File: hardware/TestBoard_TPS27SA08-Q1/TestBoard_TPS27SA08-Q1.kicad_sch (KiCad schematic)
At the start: 78 parts, among them J1 575-4, J10 Conn_01x04, J11 Conn_01x02, J12 Conn_01x02, J14 Conn_01x02, J15 Conn_01x06, J2 575-4, J3 575-4, J4 575-4, J7 Conn_01x02, J8 Conn_01x02, J9 Conn_01x02, Q1 SQJ141ELP, U1 TPS27SA08-Q1, U2 Logic Analyzer, U3 MCP23S17-E/SO, U4 NUCLEO_L432KC

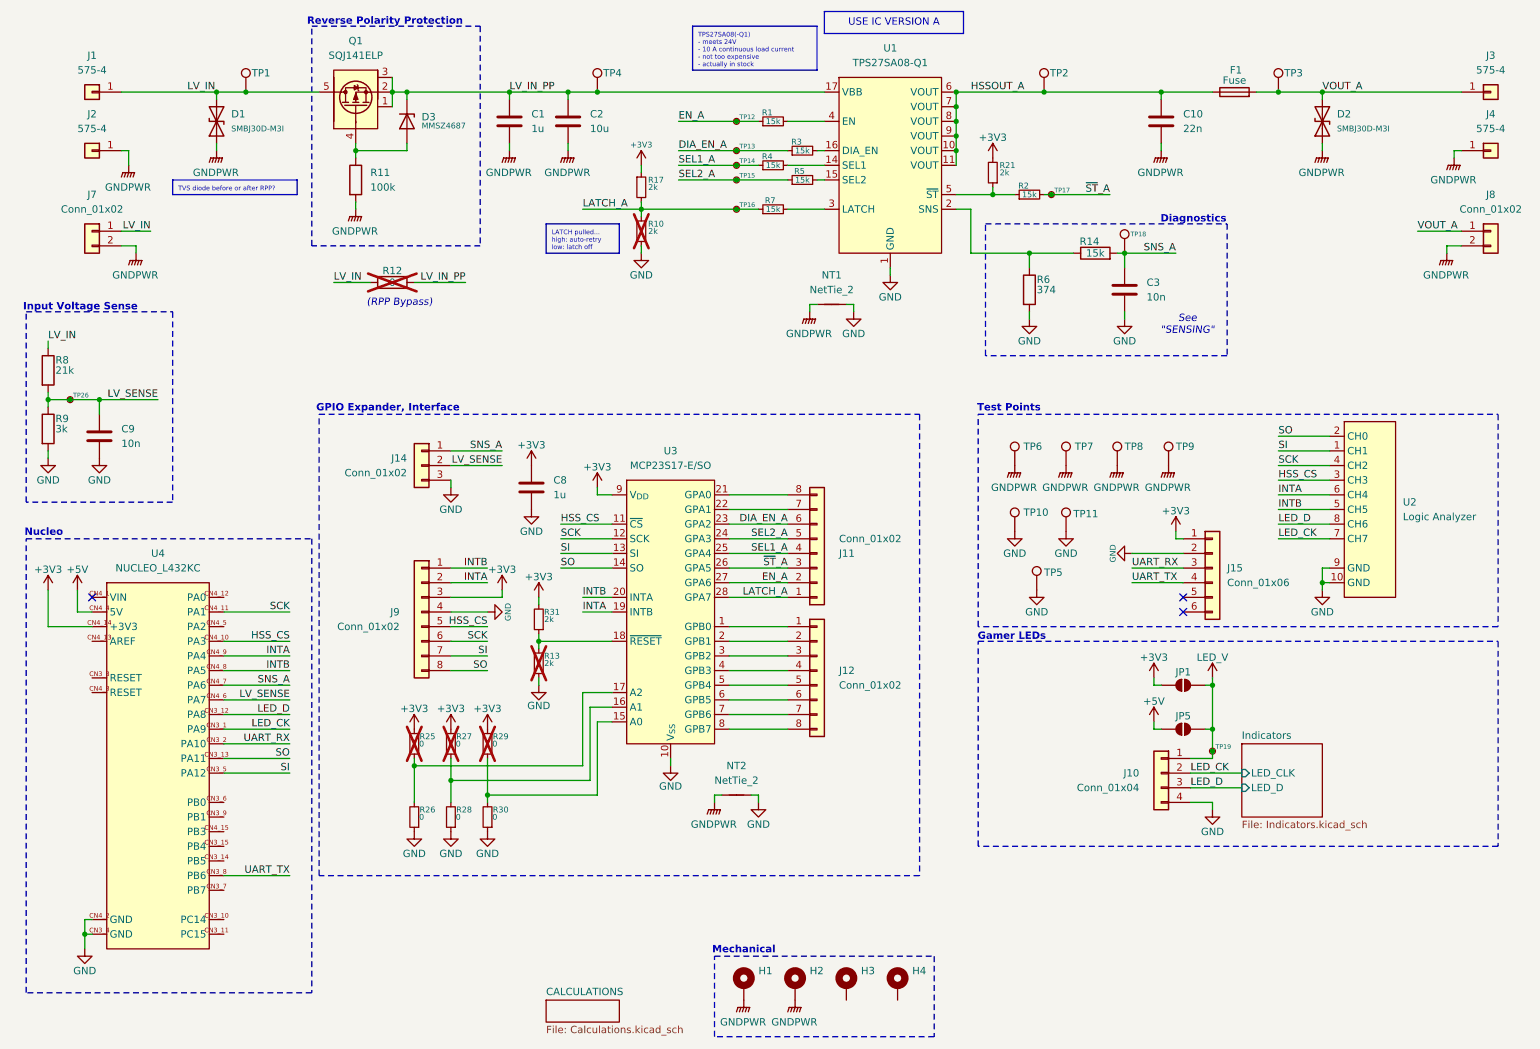
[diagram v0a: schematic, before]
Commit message: revisions (dip switch for address, leds on gpio outputs, logic analyzer pinout?, ...)
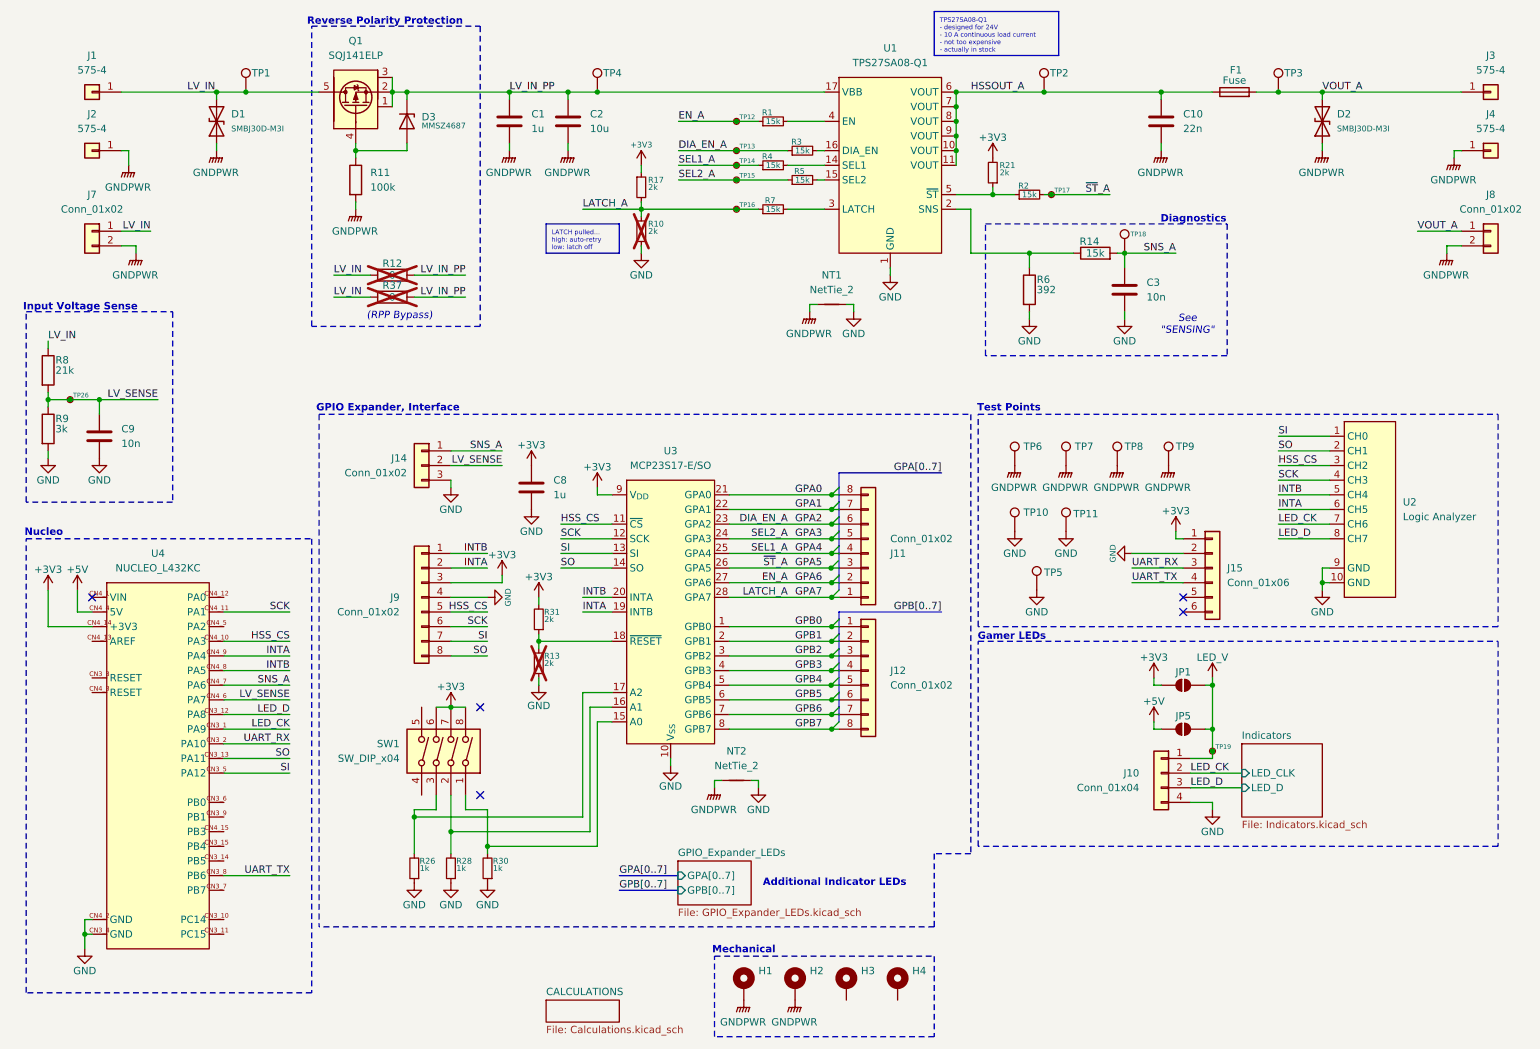
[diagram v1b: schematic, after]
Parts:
- removed R25, R27, R29: 0, Resistor_SMD:R_0805_2012Metric, symbol Device:R_Small
- added R37: 0, Resistor_SMD:R_0805_2012Metric, symbol Device:R
- added SW1: SW_DIP_x04, PowerDistributionUnitLib:ADE04S04, symbol Switch:SW_DIP_x04
- R26, R28, R30: value 0 -> 1k
- R6: value 374 -> 392
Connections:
- net +3V3: now also SW1.6, SW1.7, SW1.8
- net LV_IN: now also R37.1
- net LV_IN_PP: now also R37.2
- net at R30.2, U3.15 (A0): now also SW1.1
- net GPA1: now reaches J11.7 (Pin_7), U3.22 (GPA1)
- net GPA0: now reaches J11.8 (Pin_8), U3.21 (GPA0)
- net at R28.2, U3.16 (A1): now also SW1.2
- net GPB0: now reaches J12.1 (Pin_1), U3.1 (GPB0)
- net GPB1: now reaches J12.2 (Pin_2), U3.2 (GPB1)
- net GPB2: now reaches J12.3 (Pin_3), U3.3 (GPB2)
- net GPB3: now reaches J12.4 (Pin_4), U3.4 (GPB3)
- net GPB4: now reaches J12.5 (Pin_5), U3.5 (GPB4)
- net GPB5: now reaches J12.6 (Pin_6), U3.6 (GPB5)
- net GPB6: now reaches J12.7 (Pin_7), U3.7 (GPB6)
- net GPB7: now reaches J12.8 (Pin_8), U3.8 (GPB7)
- net at R26.2, U3.17 (A2): now also SW1.3
- net LATCH_A renamed GPA7
- net SEL1_A renamed GPA4
- net SEL2_A renamed GPA3
- net ~{ST}_A renamed GPA5
- no-connect marks 3 -> 5
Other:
- added sheet GPIO_Expander_LEDs (GPIO_Expander_LEDs.kicad_sch)
- note added: "Additional Indicator LEDs"
- moved on the sheet: J11, J12, J9, NT2, R12, R26, R28, R30

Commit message: logic analyzer fix and other little things
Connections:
- net GND: now also U2.1 (GND), U2.2 (GND); no longer U2.10 (GND), U2.9 (GND)
- net HSS_CS: now also U2.5 (CH5); no longer U2.3 (CH2)
- net INTA: now also U2.8 (CH2); no longer U2.6 (CH5)
- net INTB: now also U2.7 (CH3); no longer U2.5 (CH4)
- net LED_CK: now also U2.9 (CH1); no longer U2.7 (CH6)
- net LED_D: now also U2.10 (CH0); no longer U2.8 (CH7)
- net SCK: now also U2.6 (CH4); no longer U2.4 (CH3)
- net SI: now also U2.3 (CH7); no longer U2.1 (CH0)
- net SO: now also U2.4 (CH6); no longer U2.2 (CH1)
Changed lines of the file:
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@@
 	)
 	(label "SI"
-		(at 234.95 91.44 0)
+		(at 234.95 109.22 0)
 		(effects
 			(font
@@
 	)
 	(label "SCK"
-		(at 234.95 99.06 0)
+		(at 234.95 101.6 0)
 		(effects
 			(font
@@
 	)
 	(label "LED_D"
-		(at 234.95 109.22 0)
+		(at 234.95 91.44 0)
 		(effects
 			(font
@@
 	)
 	(label "SO"
-		(at 234.95 93.98 0)
+		(at 234.95 106.68 0)
 		(effects
 			(font
@@
 	)
 	(label "HSS_CS"
-		(at 234.95 96.52 0)
+		(at 234.95 104.14 0)
 		(effects
 			(font
@@
 	)
 	(label "INTA"
-		(at 234.95 104.14 0)
+		(at 234.95 96.52 0)
 		(effects
 			(font
@@
 	)
 	(label "INTB"
-		(at 234.95 101.6 0)
+		(at 234.95 99.06 0)
 		(effects
 			(font
@@
 	)
 	(label "LED_CK"
-		(at 234.95 106.68 0)
-		(effects
-			(font
+		(at 234.95 93.98 0)
+		(effects
+			(font

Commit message: last revisions, export gerbers and pdf schematic
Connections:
- net INTA: now also J9.1 (Pin_1), U2.7 (CH3), U3.20 (INTA), U4.CN4_8 (PA5); no longer J9.2 (Pin_2), U2.8 (CH2), U3.19 (INTB), U4.CN4_9 (PA4)
- net INTB: now also J9.2 (Pin_2), U2.8 (CH2), U3.19 (INTB), U4.CN4_9 (PA4); no longer J9.1 (Pin_1), U2.7 (CH3), U3.20 (INTA), U4.CN4_8 (PA5)
- no-connect marks 5 -> 16
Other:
- moved on the sheet: R1, R10, R17, R4, R7, TP12, TP13, TP14, TP15, TP16
